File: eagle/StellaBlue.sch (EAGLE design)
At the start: 89 parts, among them IC1 74LS245N, IC2 74LS245N, IC3 74LS245N, IC5 7805TV, T1 2N3906, T2 2N3904, T3 2N3906, T4 2N3904, X1 FMS6141

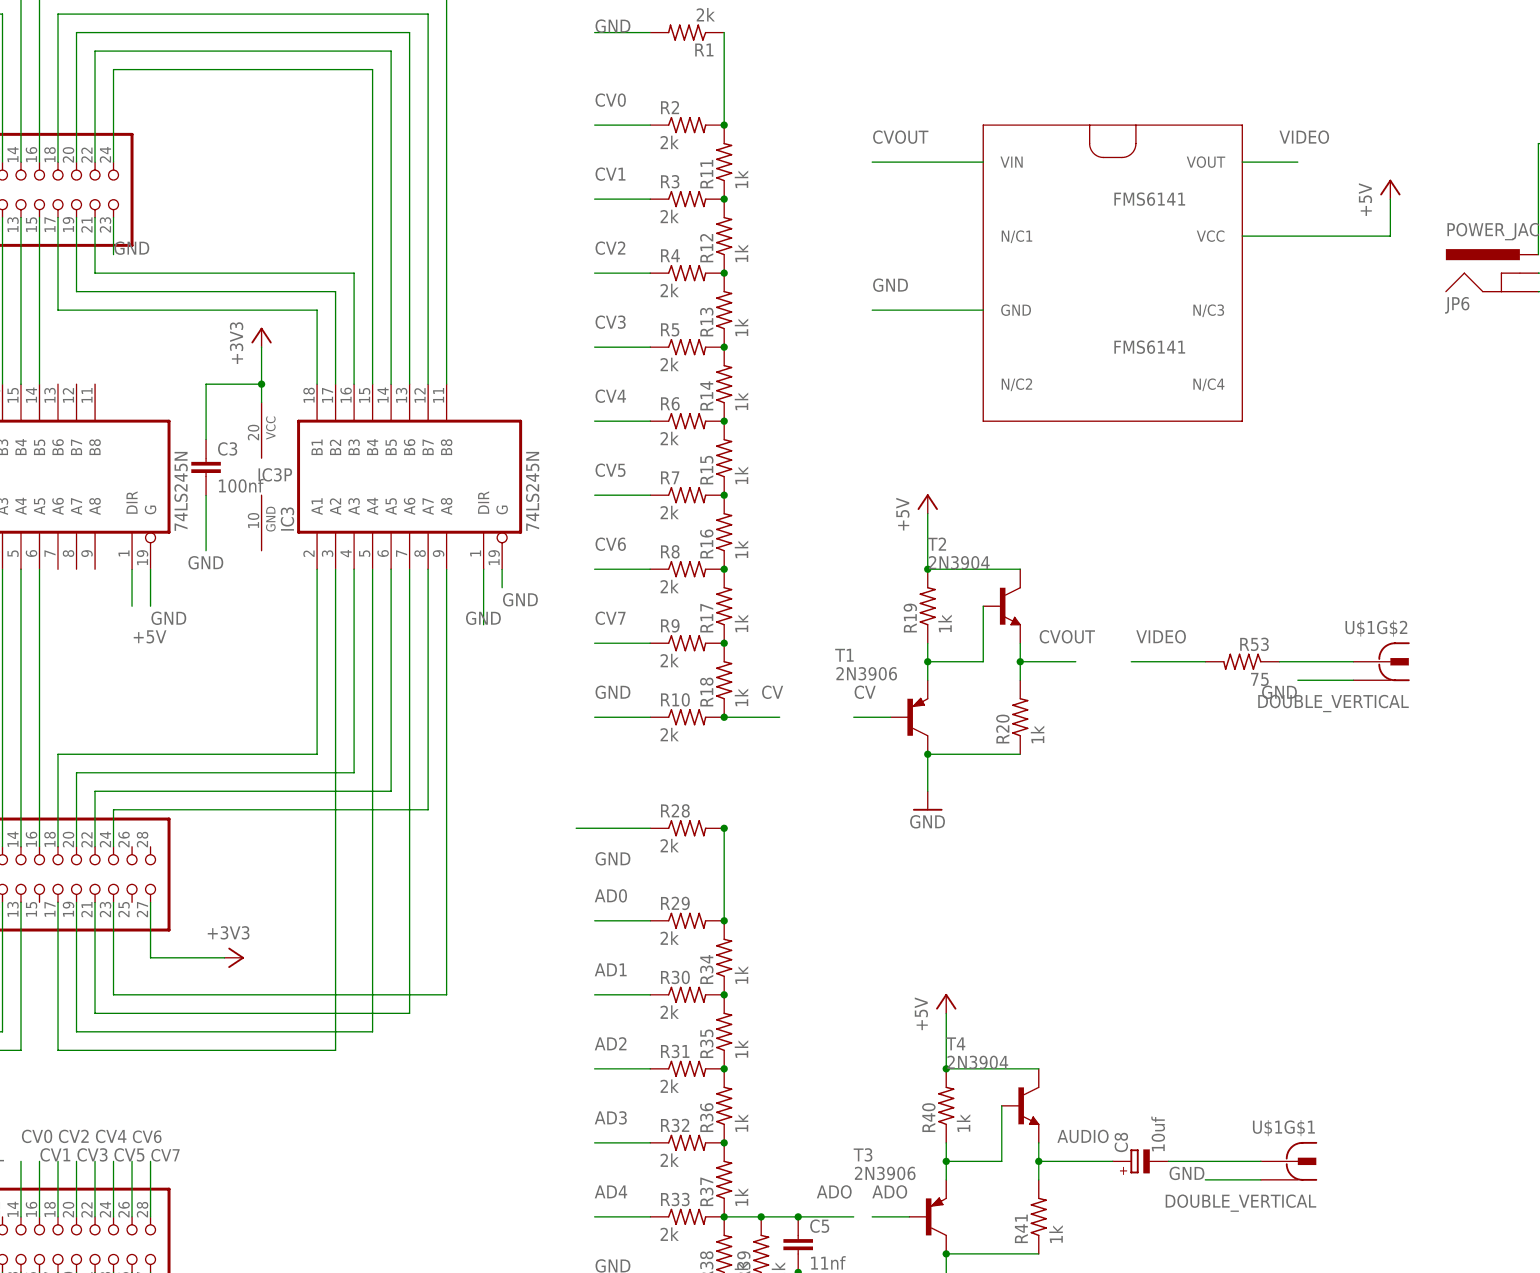
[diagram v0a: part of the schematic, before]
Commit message: labels replacement
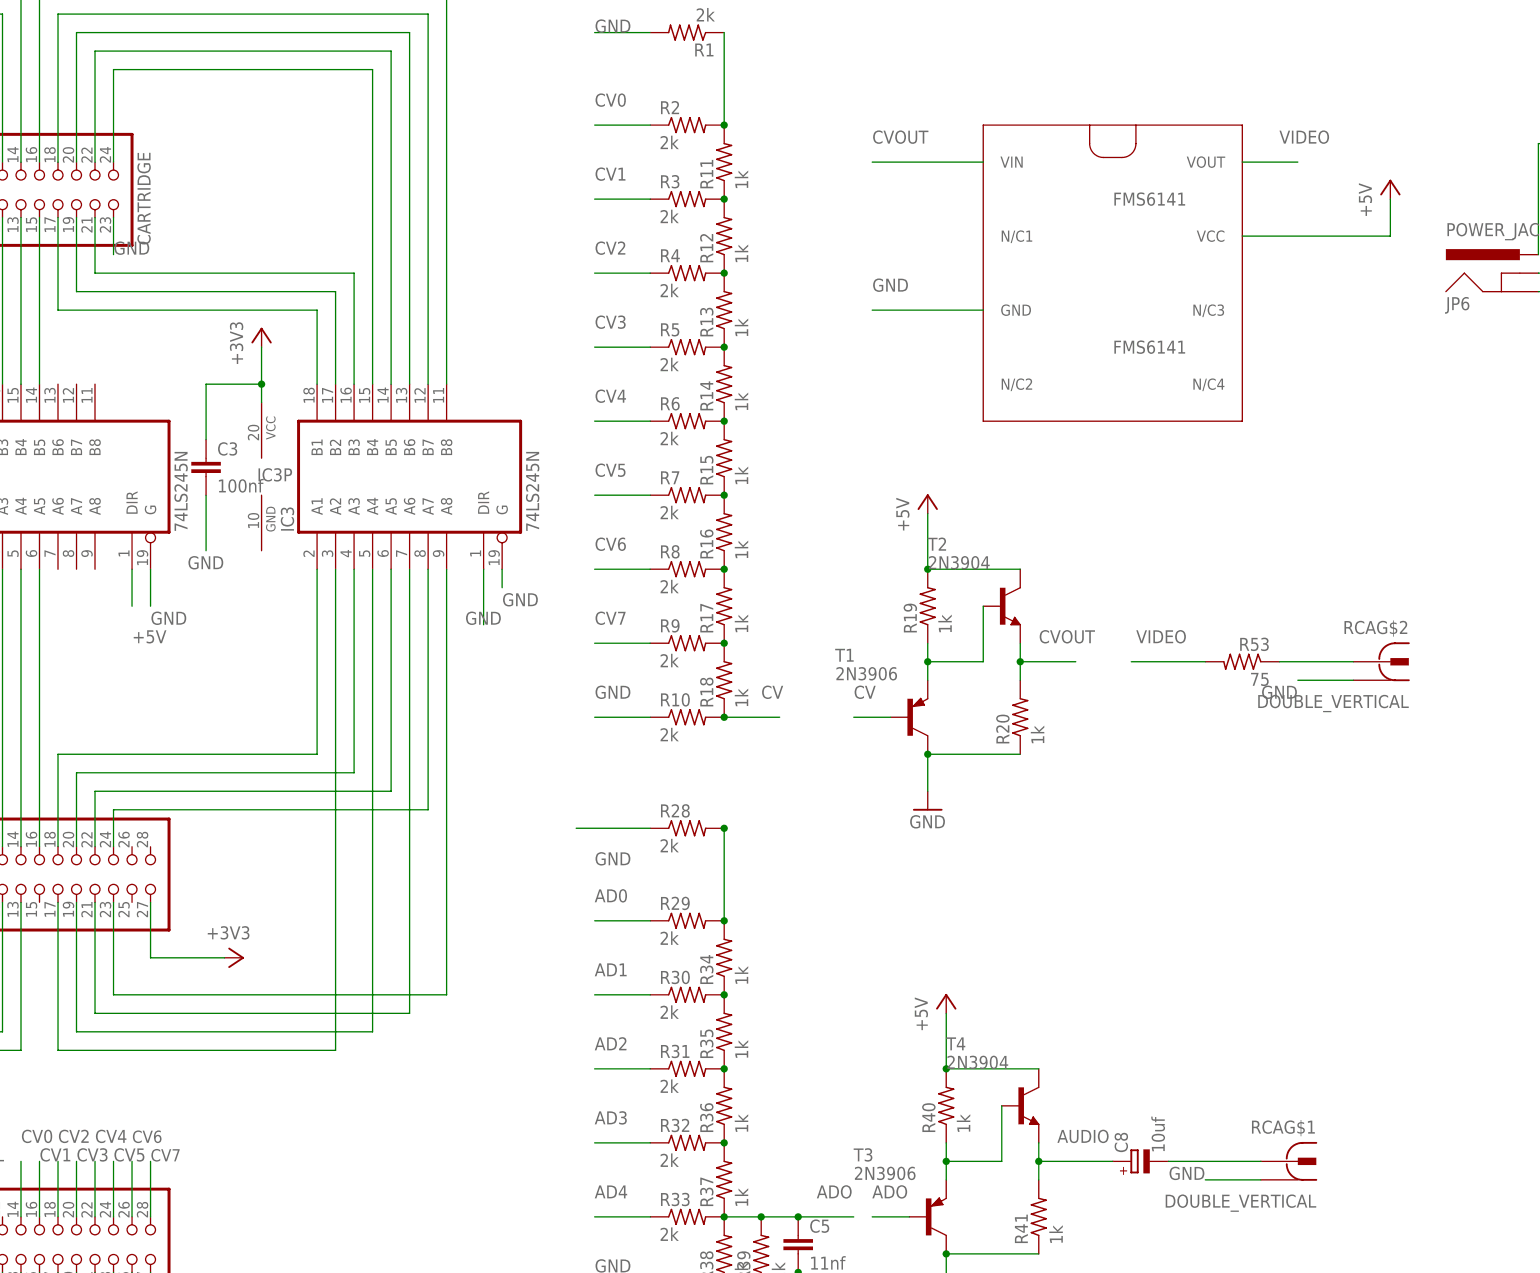
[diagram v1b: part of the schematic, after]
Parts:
- JP1: value (none) -> CARTRIDGE
- renumbered U$1 to RCA

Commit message: labels positioning
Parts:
- JP1: value CARTRIDGE -> CARTRIDGE SOCKET
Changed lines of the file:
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@@
 </classes>
 <parts>
-<part name="JP1" library="atari2600 card edge" deviceset="ATARI2600_SLOT" device="" value="CARTRIDGE"/>
+<part name="JP1" library="atari2600 card edge" deviceset="ATARI2600_SLOT" device="" value="CARTRIDGE SOCKET"/>
 <part name="JP2" library="pinhead" deviceset="PINHD-2X14" device=""/>
 <part name="JP4" library="pinhead" deviceset="PINHD-2X14" device=""/>

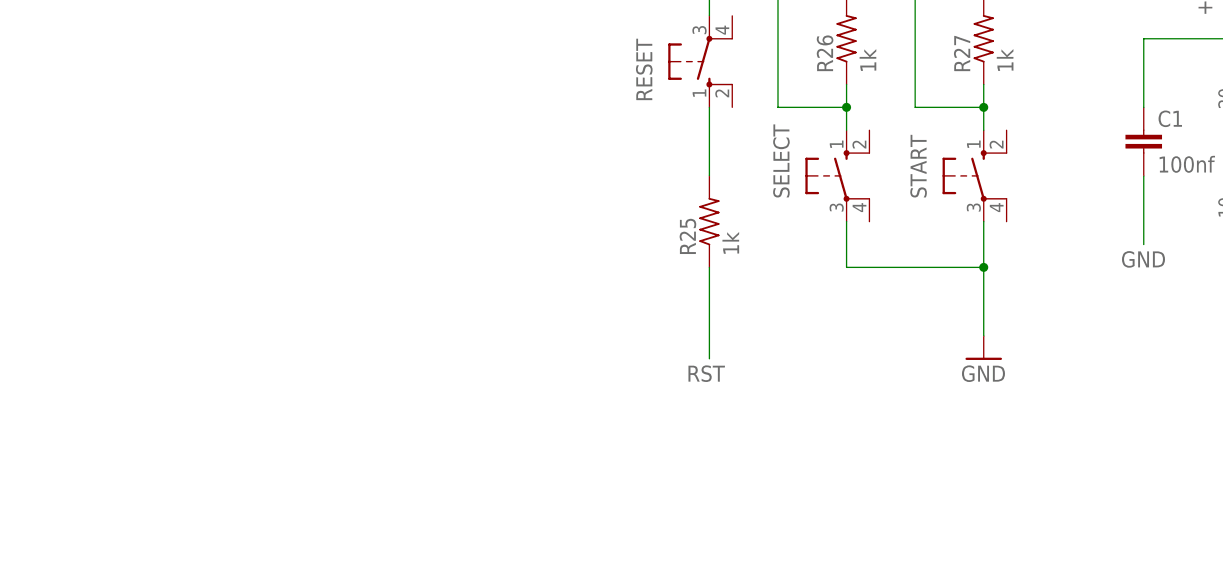
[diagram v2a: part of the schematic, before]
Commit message: First PCB routing !
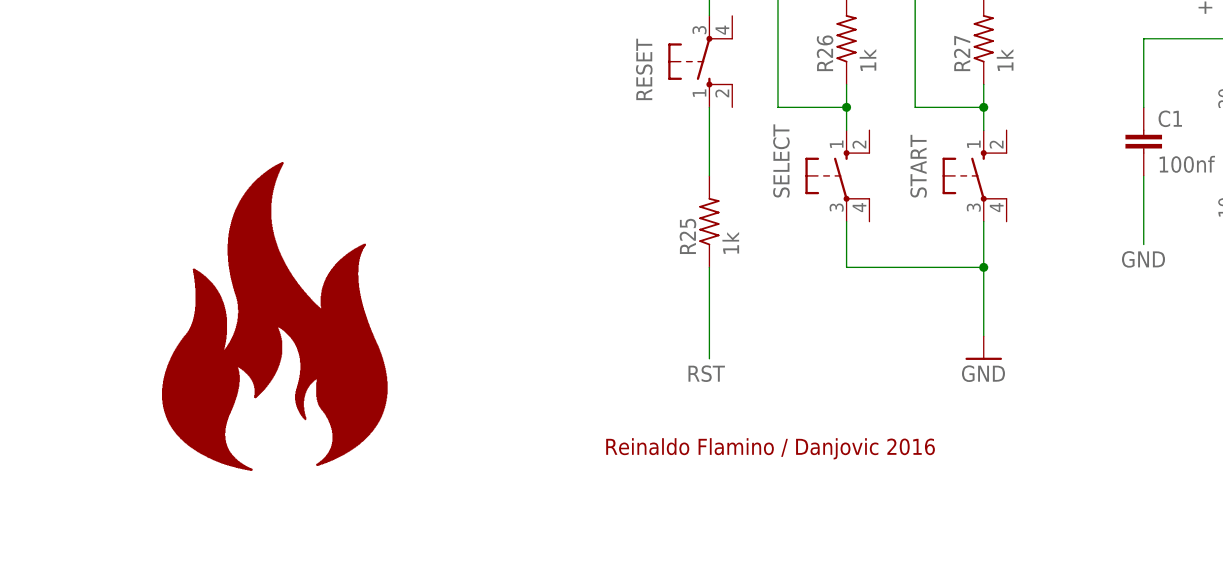
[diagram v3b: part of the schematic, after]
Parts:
- renumbered X1 to IC4
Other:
- note added: "Reinaldo Flamino / Danjovic 2016"

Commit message: Added 14.318MHz crystal oscillator
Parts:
- added C9: 10nf, capacitor-wima:C5/2.5
- added XO1: 14.318MHz, crystal:SM77H
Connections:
- new net 14.318MHZ: JP5.16, XO1.OUT
- net +3V3: now also C9.1, XO1.E/D, XO1.VCC
- net GND: now also C9.2, XO1.GND
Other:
- moved on the sheet: C4, C5, C6, C7, C8, D1, HS1, IC5, JP3, JP6, PWR, R1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
